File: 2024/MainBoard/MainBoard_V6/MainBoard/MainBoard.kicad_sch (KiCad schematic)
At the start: 101 parts, among them J1 Raspberry_Pi_2_3, J11 //ADC2, J12 //ADC2, J13 //Drib, J14 UART, J15 TFT3, J16 CAN_CON, J2 fan, J3 USB_C_Receptacle_USB2.0_16P, J4 metor, J6 Debug, J7 //ADC0, J8 MOLEX MINISPOX, Q1 Q_NMOS_GSD, Q2 Q_NMOS_GSD, SW1 SW_MEC_5E, SW2 Ras_1, SW3 Ras_2, SW4 SW_Wuerth_450301014042, SW5 SW_MEC_5E, SW6 SW_MEC_5E, U1 STM32F446RETx, U10 MPU9250, U11 LM1084-5.0, U2 CH340E, U3 MOUDLE-SEEEDUINO-XIAO, U6 BNO055, U7 AZ1117-3.3, U8 MAX3051, Y1 CSTNE16M0V530000R0

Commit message: 完成
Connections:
- net Kicker renamed discharge
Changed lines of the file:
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@@
     )
   )
-  (global_label "Kicker" (shape bidirectional) (at 86.36 104.14 180) (fields_autoplaced)
+  (global_label "discharge" (shape bidirectional) (at 86.36 104.14 180) (fields_autoplaced)
     (effects (font (size 1.27 1.27)) (justify right))
-    (property "Intersheetrefs" "${INTERSHEET_REFS}" (at 76.3972 104.14 0)
+    (property "Intersheetrefs" "${INTERSHEET_REFS}" (at 73.0712 104.14 0)
       (effects (font (size 1.27 1.27)) (justify right) hide)
     )
@@
     )
   )
-  (global_label "Kicker" (shape bidirectional) (at 234.95 133.35 0) (fields_autoplaced)
+  (global_label "discharge" (shape bidirectional) (at 234.95 133.35 0) (fields_autoplaced)
     (effects (font (size 1.27 1.27)) (justify left))
-    (property "Intersheetrefs" "${INTERSHEET_REFS}" (at 244.9128 133.35 0)
+    (property "Intersheetrefs" "${INTERSHEET_REFS}" (at 248.2388 133.35 0)
       (effects (font (size 1.27 1.27)) (justify left) hide)
     )

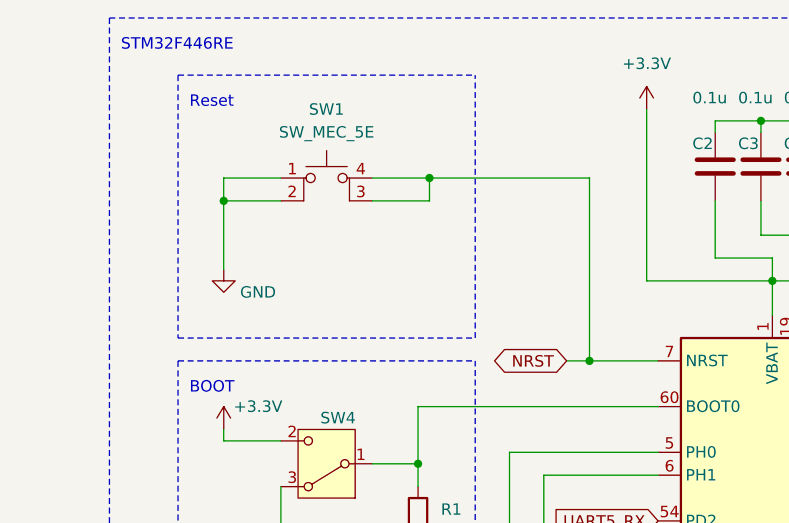
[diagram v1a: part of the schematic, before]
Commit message: 差し替えver
リセットにプルアップ抵抗いれた
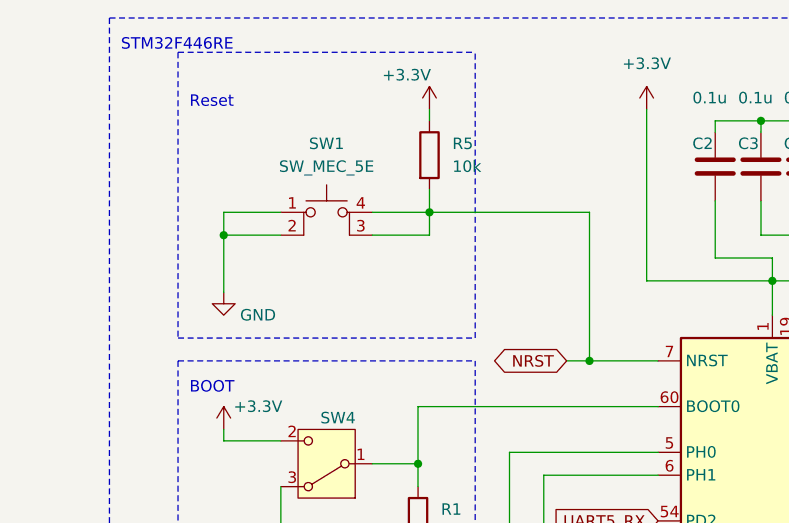
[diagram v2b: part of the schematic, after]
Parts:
- added R5: 10k, Resistor_SMD:R_0603_1608Metric_Pad0.98x0.95mm_HandSolder, symbol Device:R
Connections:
- net +3.3V: now also R5.1
- net NRST: now also R5.2
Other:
- moved on the sheet: SW1
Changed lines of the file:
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@@
     (comment 2 "Riku Miyazaki")
   )
-  (junction (at 60.96 43.18) (diameter 0) (color 0 0 0 0)
-  )
   (junction (at 256.54 73.66) (diameter 0) (color 0 0 0 0)
   )
@@
   (junction (at 208.28 135.89) (diameter 0) (color 0 0 0 0)
   )
-  (junction (at 38.1 45.72) (diameter 0) (color 0 0 0 0)
-  )
   (junction (at 118.11 36.83) (diameter 0) (color 0 0 0 0)
   )
@@
   (junction (at 157.48 135.89) (diameter 0) (color 0 0 0 0)
   )
+  (junction (at 60.96 46.99) (diameter 0) (color 0 0 0 0)
+  )
   (junction (at 113.03 36.83) (diameter 0) (color 0 0 0 0)
   )
@@
   (junction (at 58.42 218.44) (diameter 0) (color 0 0 0 0)
   )
+  (junction (at 38.1 49.53) (diameter 0) (color 0 0 0 0)
+  )
   (junction (at 237.49 63.5) (diameter 0) (color 0 0 0 0)
   )
@@
     (stroke (width 0) (type default))
   )
-  (wire (pts (xy 38.1 45.72) (xy 44.45 45.72))
+  (wire (pts (xy 38.1 49.53) (xy 44.45 49.53))
     (stroke (width 0) (type default))
   )
@@
     (stroke (width 0) (type default))
   )
+  (wire (pts (xy 60.96 44.45) (xy 60.96 46.99))
+    (stroke (width 0) (type default))
+  )
   (wire (pts (xy 285.75 173.99) (xy 308.61 173.99))
     (stroke (width 0) (type default))
@@
     (stroke (width 0) (type default))
   )
+  (wire (pts (xy 60.96 35.56) (xy 60.96 36.83))
+    (stroke (width 0) (type default))
+  )
   (wire (pts (xy 370.84 69.85) (xy 391.16 69.85))
     (stroke (width 0) (type default))
@@
     (stroke (width 0) (type default))
   )
+  (wire (pts (xy 38.1 49.53) (xy 38.1 55.88))
+    (stroke (width 0) (type default))
+  )
   (polyline (pts (xy 66.04 93.98) (xy 66.04 63.5))
     (stroke (width 0) (type dash))
@@
     (stroke (width 0) (type default))
   )
-  (wire (pts (xy 60.96 43.18) (xy 78.74 43.18))
-    (stroke (width 0) (type default))
-  )
   (wire (pts (xy 496.57 205.74) (xy 496.57 209.55))
     (stroke (width 0) (type default))
@@
     (stroke (width 0) (type default))
   )
-  (polyline (pts (xy 33.02 31.75) (xy 33.02 60.96))
+  (polyline (pts (xy 33.02 29.21) (xy 33.02 60.96))
     (stroke (width 0) (type dash))
   )
@@
     (stroke (width 0) (type default))
   )
-  (wire (pts (xy 44.45 43.18) (xy 38.1 43.18))
+  (wire (pts (xy 44.45 46.99) (xy 38.1 46.99))
     (stroke (width 0) (type default))
   )
@@
     (stroke (width 0) (type default))
   )
-  (wire (pts (xy 54.61 43.18) (xy 60.96 43.18))
-    (stroke (width 0) (type default))
-  )
-  (wire (pts (xy 38.1 45.72) (xy 38.1 53.34))
+  (wire (pts (xy 54.61 46.99) (xy 60.96 46.99))
     (stroke (width 0) (type default))
   )
@@
     (stroke (width 0) (type default))
   )
+  (wire (pts (xy 60.96 46.99) (xy 78.74 46.99))
+    (stroke (width 0) (type default))
+  )
   (wire (pts (xy 494.03 102.87) (xy 494.03 101.6))
     (stroke (width 0) (type default))
@@
     (stroke (width 0) (type dash))
   )
-  (wire (pts (xy 78.74 43.18) (xy 78.74 63.5))
-    (stroke (width 0) (type default))
-  )
   (wire (pts (xy 408.94 123.19) (xy 414.02 123.19))
     (stroke (width 0) (type default))
@@
     (stroke (width 0) (type default))
   )
-  (polyline (pts (xy 66.04 60.96) (xy 66.04 31.75))
+  (polyline (pts (xy 66.04 60.96) (xy 66.04 29.21))
     (stroke (width 0) (type dash))
   )
@@
     (stroke (width 0) (type default))
   )
-  (polyline (pts (xy 33.02 31.75) (xy 66.04 31.75))
+  (polyline (pts (xy 33.02 29.21) (xy 66.04 29.21))
     (stroke (width 0) (type dash))
   )
@@
     (stroke (width 0) (type default))
   )
-  (wire (pts (xy 60.96 43.18) (xy 60.96 45.72))
+  (wire (pts (xy 60.96 46.99) (xy 60.96 49.53))
     (stroke (width 0) (type default))
   )
@@
     (stroke (width 0) (type default))
   )
-  (wire (pts (xy 38.1 43.18) (xy 38.1 45.72))
+  (wire (pts (xy 38.1 46.99) (xy 38.1 49.53))
     (stroke (width 0) (type default))
   )
@@
     (stroke (width 0) (type default))
   )
+  (wire (pts (xy 78.74 46.99) (xy 78.74 63.5))
+    (stroke (width 0) (type default))
+  )
   (wire (pts (xy 248.92 43.18) (xy 240.03 43.18))
     (stroke (width 0) (type default))
@@
     (stroke (width 0) (type default))
   )
-  (wire (pts (xy 54.61 45.72) (xy 60.96 45.72))
+  (wire (pts (xy 54.61 49.53) (xy 60.96 49.53))
     (stroke (width 0) (type default))
   )
@@
     )
   )
-  (symbol (lib_id "power:GND") (at 38.1 53.34 0) (unit 1)
+  (symbol (lib_id "power:GND") (at 38.1 55.88 0) (unit 1)
     (in_bom yes) (on_board yes) (dnp no)
-    (property "Reference" "#PWR08" (at 38.1 59.69 0)
+    (property "Reference" "#PWR08" (at 38.1 62.23 0)
       (effects (font (size 1.27 1.27)) hide)
     )
-    (property "Value" "GND" (at 41.91 55.88 0)
+    (property "Value" "GND" (at 41.91 58.42 0)
       (effects (font (size 1.27 1.27)))
     )
-    (property "Footprint" "" (at 38.1 53.34 0)
+    (property "Footprint" "" (at 38.1 55.88 0)
       (effects (font (size 1.27 1.27)) hide)
     )
-    (property "Datasheet" "" (at 38.1 53.34 0)
+    (property "Datasheet" "" (at 38.1 55.88 0)
       (effects (font (size 1.27 1.27)) hide)
     )
@@
     )
   )
-  (symbol (lib_id "Switch:SW_MEC_5E") (at 49.53 45.72 0) (unit 1)
+  (symbol (lib_id "Switch:SW_MEC_5E") (at 49.53 49.53 0) (unit 1)
     (in_bom yes) (on_board yes) (dnp no) (fields_autoplaced)
-    (property "Reference" "SW1" (at 49.53 35.56 0)
+    (property "Reference" "SW1" (at 49.53 39.37 0)
       (effects (font (size 1.27 1.27)))
     )
-    (property "Value" "SW_MEC_5E" (at 49.53 38.1 0)
+    (property "Value" "SW_MEC_5E" (at 49.53 41.91 0)
       (effects (font (size 1.27 1.27)))
     )
-    (property "Footprint" "MainBoard:SW_SKRPACE010" (at 49.53 38.1 0)
+    (property "Footprint" "MainBoard:SW_SKRPACE010" (at 49.53 41.91 0)
       (effects (font (size 1.27 1.27)) hide)
     )
-    (property "Datasheet" "http://www.apem.com/int/index.php?controller=attachment&id_attachment=1371" (at 49.53 38.1 0)
+    (property "Datasheet" "http://www.apem.com/int/index.php?controller=attachment&id_attachment=1371" (at 49.53 41.91 0)
       (effects (font (size 1.27 1.27)) hide)
     )
@@
     )
   )
+  (symbol (lib_id "power:+3.3V") (at 60.96 35.56 0) (unit 1)
+    (in_bom yes) (on_board yes) (dnp no)
+    (property "Reference" "#PWR073" (at 60.96 39.37 0)
+      (effects (font (size 1.27 1.27)) hide)
+    )
+    (property "Value" "+3.3V" (at 58.42 31.75 0)
+      (effects (font (size 1.27 1.27)))
+    )
+    (property "Footprint" "" (at 60.96 35.56 0)
+      (effects (font (size 1.27 1.27)) hide)
+    )
+    (property "Datasheet" "" (at 60.96 35.56 0)
+      (effects (font (size 1.27 1.27)) hide)
+    )
+    (pin "1")
+    (instances
+      (project "MainBoard"
+        (path "/0f1369eb-a284-48b8-a3ed-798a8062c1cf"
+          (reference "#PWR073") (unit 1)
+        )
+      )
+    )
+  )
   (symbol (lib_id "Device:LED") (at 534.67 193.04 90) (unit 1)
     (in_bom yes) (on_board yes) (dnp no)
@@
         )
       )
+    )
+  )
+  (symbol (lib_id "Device:R") (at 60.96 40.64 0) (unit 1)
+    (in_bom yes) (on_board yes) (dnp no) (fields_autoplaced)
+    (property "Reference" "R5" (at 63.5 39.37 0)
+      (effects (font (size 1.27 1.27)) (justify left))
+    )
+    (property "Value" "10k" (at 63.5 41.91 0)
+      (effects (font (size 1.27 1.27)) (justify left))
+    )
+    (property "Footprint" "Resistor_SMD:R_0603_1608Metric_Pad0.98x0.95mm_HandSolder" (at 59.182 40.64 90)
+      (effects (font (size 1.27 1.27)) hide)
+    )
+    (property "Datasheet" "~" (at 60.96 40.64 0)
+      (effects (font (size 1.27 1.27)) hide)
+    )
+    (pin "1")
+    (pin "2")
+    (instances
+      (project "MainBoard"
+        (path "/0f1369eb-a284-48b8-a3ed-798a8062c1cf"
+          (reference "R5") (unit 1)
+        )
+      )
